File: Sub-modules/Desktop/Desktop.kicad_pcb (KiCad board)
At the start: 2 copper layers, 60 x 43 mm, 58 parts, among them J1 USB_C_Receptacle_USB2.0_14P, J2 PR5L5015-5P-C-H, J3 PR5L5015-5P-C-H, SW1 SKRPACE010, SW2 SW_Push, SW3 SKRPACE010, U1 W25Q16JVSS, U10 AT24CS02-SSHM, U2 MAX40200AUK, U3 RP2040, U4 TLV75733PDBV, U5 STCC4, U6 STHS34PF80, U7 VEML7700-TT, U8 MCP79410, U9 SHT40, Y1 ABM8-272-T3, Y2 X1A0000610006

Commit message: Added silkscreen
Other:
- board text added: "07/26"
- board text added: "BOOTSEL"
- board text added: "ESP-HI-PLUS Desktop v1"
- board text added: "JLCJLCJLCJLC"
- board text added: "MAG1"
- board text added: "MAG2"
- board text added: "RESET"

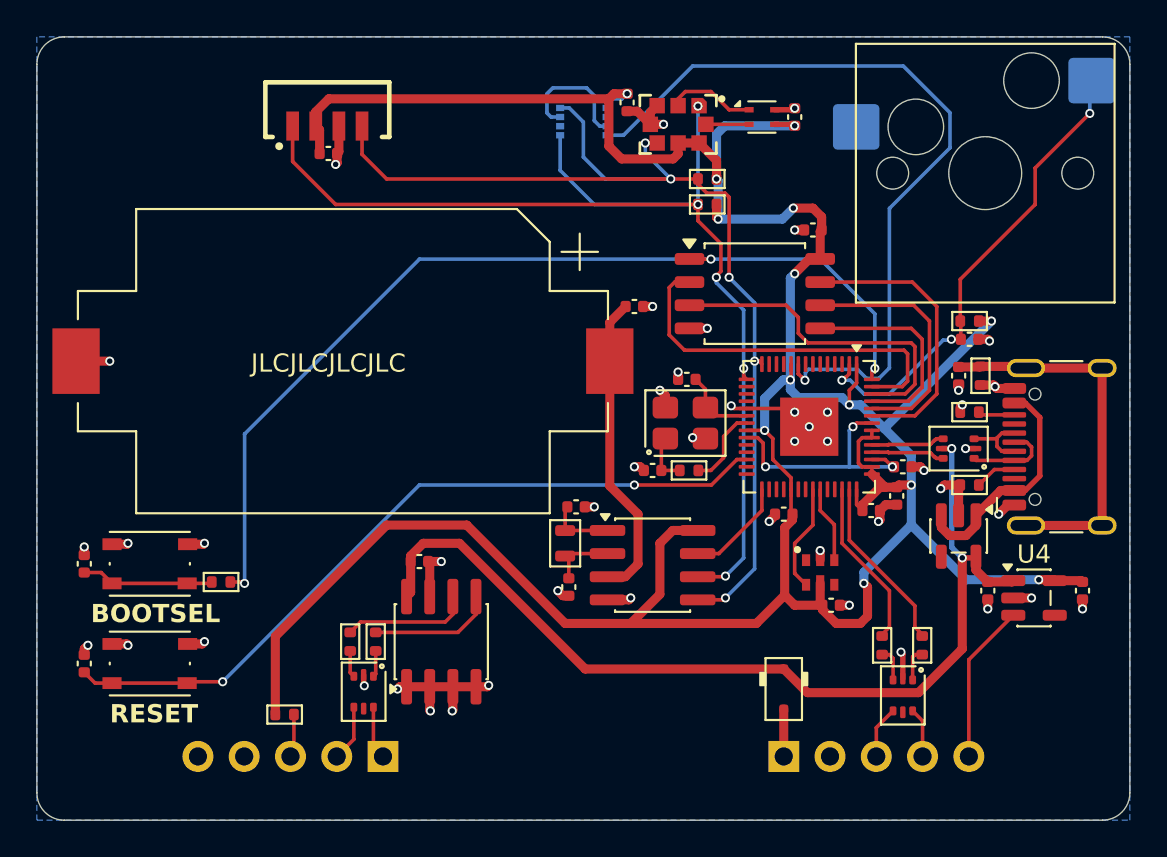
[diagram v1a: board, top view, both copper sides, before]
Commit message: Desktop v1.1: changed CO2 sensor to SCD40 changed location and orientation of presence sensor
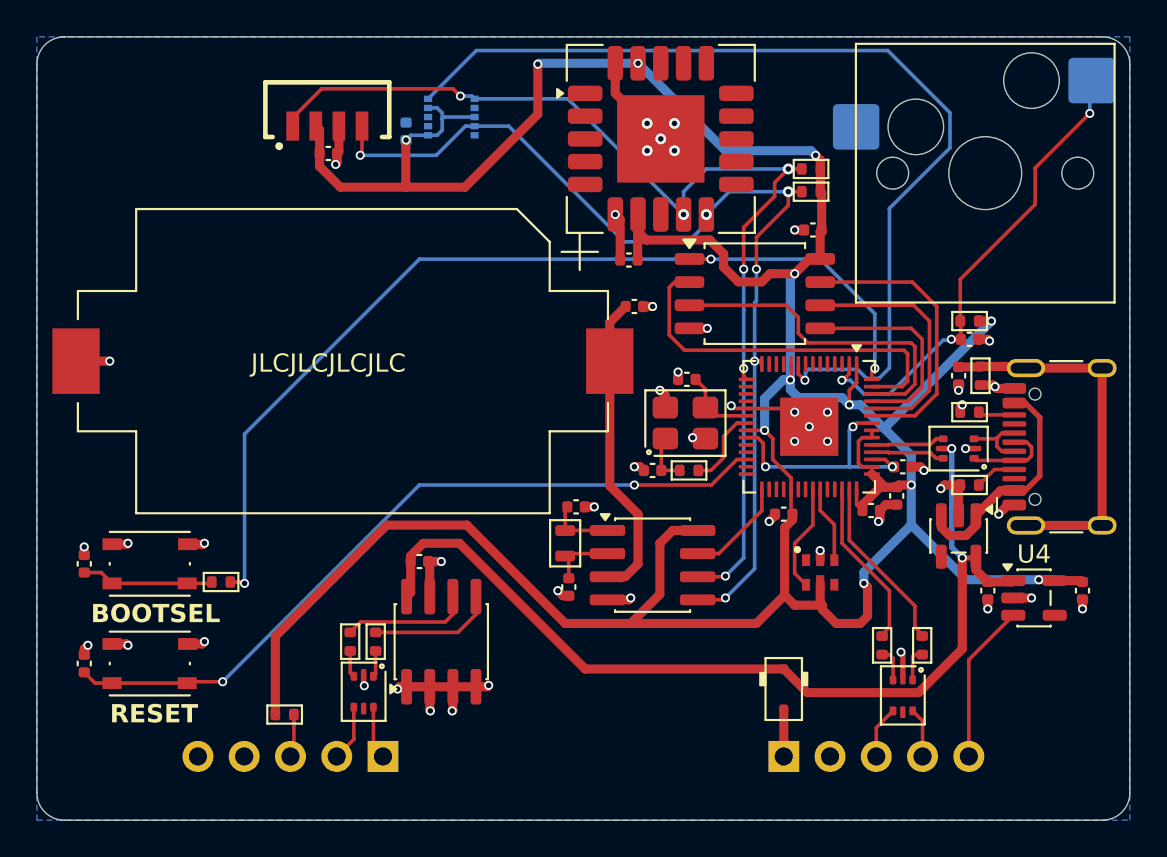
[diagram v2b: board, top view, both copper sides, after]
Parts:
- removed C17: 0u1, Capacitor_SMD:C_0402_1005Metric
- removed U9: SHT40, Sensor_Humidity:Sensirion_DFN-4_1.5x1.5mm_P0.8mm_SHT4x_NoCentralPad
- C16: moved to B.Cu
- U5: value STCC4 -> SCD40-D-R2; footprint PCM_SparkFun-Sensor:STCC4 -> Sensor:Sensirion_SCD4x-1EP_10.1x10.1mm_P1.25mm_EP4.8x4.8mm
- moved C11 22.0 mm to (131.5, 55.2), turned to 0 degrees
- moved C16 12.2 mm to (119.3, 48.2), turned to -90 degrees
- moved U6 7.25 mm to (121.8, 47.4), turned to 180 degrees
- moved R8 6.02 mm to (141.5, 50.2)
- moved R7 5.74 mm to (141.5, 51.5)
- moved U5 1.24 mm to (133.2, 48.6), turned to 0 degrees
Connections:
- U5 pad 1: /RP_I2C_SCL -> (no net)
- U5 pad 2: Net-(U5-SDA_C) -> (no net)
- U5 pad 3: GND -> (no net)
- U5 pad 4: GND -> (no net)
- U5 pad 5: /RP_I2C_SDA -> (no net)
- U5 pad 6: +3V3 -> GND
- U5 pad 8: Net-(U5-SCL_C) -> (no net)
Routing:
- net /PS_INT: track 43.5 -> 53.2 mm
- net /RP_I2C_SCL: track 65.2 -> 59.7 mm, vias 5 -> 6
- net Net-(U5-SDA_C): track 4.85 -> 0.00 mm
- net +3V3: track 184.3 -> 188.7 mm, vias 13 -> 12
- net /RP_I2C_SDA: track 60.4 -> 56.4 mm, vias 5 -> 6
- net GND: track 52.0 -> 54.6 mm, vias 48 -> 51
- net Net-(U5-SCL_C): track 2.38 -> 0.00 mm
